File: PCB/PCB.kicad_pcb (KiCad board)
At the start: 4 copper layers, 54 x 29 mm, 80 parts, among them J1 USB_B_Micro, Q1 PJA3428, Q2 PJA3428, Q3 AO3401A, SW1 SW_Push, SW2 SW_Push, SW3 SW_Push, SW4 ON/OFF, U1 ESP32-PICO-MINI-02, U2 CP2102N-Axx-xQFN24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

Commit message: label btns and tps
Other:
- board text added: "BATT+"
- board text added: "BATT-"
- board text added: "CTS"
- board text added: "DTR"
- board text added: "GPIO0"
- board text added: "RESET"
- board text added: "RTS"
- board text added: "RX"
- board text added: "SCL"
- board text added: "SDA"
- board text added: "TX"
- board text added: "VIN"
- board text added: "~{INT}"
- board text added: "~{RESET}"

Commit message: silky touch ups
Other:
- board text added: "ECE477 Fall 2022 - Team 13 Brayden McNamara Ethan Crocker Kenzie Rappe Sean Boltjes"
- board text added: "Last Modified: 10/03/2022"
- board text added: "X"
- board text added: "Y"
- board text added: "Z"
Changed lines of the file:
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@@
   (gr_circle (center 225.725 102.425) (end 225.775 102.5) (layer "B.SilkS") (width 0.15) (fill none))
   (gr_circle (center 225.8 107.075) (end 225.9 107.1) (layer "B.SilkS") (width 0.15) (fill none))
+  (gr_line (start 240.853993 110.35) (end 240.403993 110) (layer "F.SilkS") (width 0.15))
+  (gr_line (start 238.603993 108.725) (end 238.803993 108.55) (layer "F.SilkS") (width 0.15))
+  (gr_circle (center 238.803993 110.35) (end 239.303993 111.5) (layer "F.SilkS") (width 0.15) (fill none))
+  (gr_line (start 238.803993 108.775) (end 238.803993 108.325) (layer "F.SilkS") (width 0.15))
+  (gr_line (start 240.603993 110.45) (end 240.453993 110.5) (layer "F.SilkS") (width 0.15))
+  (gr_line (start 240.403993 110.05) (end 240.403993 110) (layer "F.SilkS") (width 0.15))
+  (gr_line (start 240.453993 110.5) (end 240.628993 110.35) (layer "F.SilkS") (width 0.15))
   (gr_circle (center 235.025 107.85) (end 235.125 107.9) (layer "F.SilkS") (width 0.15) (fill none))
+  (gr_line (start 238.953993 108.725) (end 238.803993 108.55) (layer "F.SilkS") (width 0.15))
+  (gr_line (start 240.082986 110.35) (end 240.378993 110.35) (layer "F.SilkS") (width 0.15))
+  (gr_line (start 240.403993 110.35) (end 240.403993 110.7) (layer "F.SilkS") (width 0.15))
+  (gr_line (start 238.503993 108.775) (end 238.453993 108.775) (layer "F.SilkS") (width 0.15))
+  (gr_line (start 240.453993 110.15) (end 240.628993 110.35) (layer "F.SilkS") (width 0.15))
+  (gr_line (start 238.903993 108.575) (end 238.953993 108.725) (layer "F.SilkS") (width 0.15))
+  (gr_line (start 240.403993 110.35) (end 240.853993 110.35) (layer "F.SilkS") (width 0.15))
+  (gr_line (start 240.403993 110.7) (end 240.403993 110.05) (layer "F.SilkS") (width 0.15))
+  (gr_line (start 240.853993 110.35) (end 240.403993 110.7) (layer "F.SilkS") (width 0.15))
+  (gr_line (start 238.803993 108.325) (end 239.153993 108.775) (layer "F.SilkS") (width 0.15))
+  (gr_line (start 238.803993 108.775) (end 239.153993 108.775) (layer "F.SilkS") (width 0.15))
+  (gr_line (start 238.803993 109.096007) (end 238.803993 108.8) (layer "F.SilkS") (width 0.15))
+  (gr_line (start 238.803993 108.325) (end 238.453993 108.775) (layer "F.SilkS") (width 0.15))
+  (gr_line (start 239.153993 108.775) (end 238.503993 108.775) (layer "F.SilkS") (width 0.15))
   (gr_line (start 245.649999 119.199999) (end 245.65 92.16) (layer "Edge.Cuts") (width 0.2))
   (gr_arc (start 245.649999 119.199999) (mid 245.357106 119.907106) (end 244.649999 120.199999) (layer "Edge.Cuts") (width 0.2))
@@
   (gr_line (start 244.65 91.2) (end 192.65 91.2) (layer "Edge.Cuts") (width 0.2))
   (gr_line (start 191.65 92.2) (end 191.65 119.2) (layer "Edge.Cuts") (width 0.2))
+  (gr_text "ECE477 Fall 2022 - Team 13\nBrayden McNamara\nEthan Crocker\nKenzie Rappe\nSean Boltjes" (at 220.9 116.15) (layer "B.SilkS")
+    (effects (font (size 0.9 0.9) (thickness 0.2)) (justify left mirror))
+  )
   (gr_text "~{INT}" (at 205.2 117.55) (layer "B.SilkS")
     (effects (font (size 0.7 0.7) (thickness 0.15)))
@@
   (gr_text "CTS\n" (at 230.35 104.15) (layer "B.SilkS")
     (effects (font (size 0.7 0.7) (thickness 0.15)))
+  )
+  (gr_text "Last Modified: 10/03/2022" (at 230.1 119.05) (layer "B.SilkS")
+    (effects (font (size 0.8 0.8) (thickness 0.15)) (justify mirror))
   )
   (gr_text "SCL\n" (at 202.55 107) (layer "F.SilkS")
@@
     (effects (font (size 0.7 0.7) (thickness 0.15)))
   )
+  (gr_text "Z" (at 238.803993 110.4) (layer "F.SilkS")
+    (effects (font (size 1.5 1.5) (thickness 0.25)))
+  )
   (gr_text "TX\n" (at 233.9 112.55) (layer "F.SilkS")
     (effects (font (size 0.7 0.7) (thickness 0.15)))
@@
     (effects (font (size 0.7 0.7) (thickness 0.15)))
   )
+  (gr_text "Y\n" (at 238.803993 107.25) (layer "F.SilkS")
+    (effects (font (size 1.5 1.5) (thickness 0.25)))
+  )
+  (gr_text "X" (at 241.453993 110.4) (layer "F.SilkS")
+    (effects (font (size 1.5 1.5) (thickness 0.25)))
+  )
   (gr_text "GPIO0" (at 222.6 100.45) (layer "F.SilkS")

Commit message: buck-boost delete
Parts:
- added R9: 100k, Resistor_SMD:R_0603_1608Metric, F.Cu at (218.0, 94.0)
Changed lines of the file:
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@@
   (net 74 "unconnected-(U1-Pad19)")
   (net 75 "unconnected-(U1-Pad24)")
+  (net 76 "Net-(U4-Pad8)")
   (footprint "Button_Switch_THT:SW_Tactile_SPST_Angled_PTS645Vx58-2LFS" (layer "F.Cu")
     (at 242.59 117.42 180)
@@
       (offset (xyz 0 0 0))
       (scale (xyz 1 1 1))
+      (rotate (xyz 0 0 0))
+    )
+  )
+  (footprint "Resistor_SMD:R_0603_1608Metric" (layer "F.Cu")
+    (at 218 94)
+    (descr "Resistor SMD 0603 (1608 Metric), square (rectangular) end terminal, IPC_7351 nominal, (Body size source: IPC-SM-782 page 72, https://www.pcb-3d.com/wordpress/wp-content/uploads/ipc-sm-782a_amendment_1_and_2.pdf), generated with kicad-footprint-generator")
+    (tags "resistor")
+    (property "Sheetfile" "PCB.kicad_sch")
+    (property "Sheetname" "")
+    (attr smd)
+    (fp_text reference "R9" (at 0 -1.43) (layer "F.SilkS")
+      (effects (font (size 1 1) (thickness 0.15)))
+    )
+    (fp_text value "100k" (at 0 1.43) (layer "F.Fab")
+      (effects (font (size 1 1) (thickness 0.15)))
+    )
+    (fp_text user "${REFERENCE}" (at 0 0) (layer "F.Fab")
+      (effects (font (size 0.4 0.4) (thickness 0.06)))
+    )
+    (fp_line (start -0.237258 0.5225) (end 0.237258 0.5225) (layer "F.SilkS") (width 0.12))
+    (fp_line (start -0.237258 -0.5225) (end 0.237258 -0.5225) (layer "F.SilkS") (width 0.12))
+    (fp_line (start -1.48 0.73) (end -1.48 -0.73) (layer "F.CrtYd") (width 0.05))
+    (fp_line (start 1.48 0.73) (end -1.48 0.73) (layer "F.CrtYd") (width 0.05))
+    (fp_line (start 1.48 -0.73) (end 1.48 0.73) (layer "F.CrtYd") (width 0.05))
+    (fp_line (start -1.48 -0.73) (end 1.48 -0.73) (layer "F.CrtYd") (width 0.05))
+    (fp_line (start -0.8 0.4125) (end -0.8 -0.4125) (layer "F.Fab") (width 0.1))
+    (fp_line (start 0.8 0.4125) (end -0.8 0.4125) (layer "F.Fab") (width 0.1))
+    (fp_line (start -0.8 -0.4125) (end 0.8 -0.4125) (layer "F.Fab") (width 0.1))
+    (fp_line (start 0.8 -0.4125) (end 0.8 0.4125) (layer "F.Fab") (width 0.1))
+    (pad "1" smd roundrect (at -0.825 0) (size 0.8 0.95) (layers "F.Cu" "F.Paste" "F.Mask") (roundrect_rratio 0.25)
+      (net 76 "Net-(U4-Pad8)") (pintype "passive"))
+    (pad "2" smd roundrect (at 0.825 0) (size 0.8 0.95) (layers "F.Cu" "F.Paste" "F.Mask") (roundrect_rratio 0.25)
+      (net 26 "Vin") (pintype "passive"))
+    (model "${KICAD6_3DMODEL_DIR}/Resistor_SMD.3dshapes/R_0603_1608Metric.wrl"
+      (offset (xyz 0 0 0))
+      (scale (xyz 1 1 1))

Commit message: buck-boost pcb
buck-boost added to pcb
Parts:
- added C12: 47uF, Capacitor_SMD:C_0603_1608Metric, F.Cu at (199.0, 100.0)
- added C13: 100nF, Capacitor_SMD:C_0603_1608Metric, F.Cu at (200.0, 95.0)
- added C14: 10uF, Capacitor_SMD:C_0603_1608Metric, F.Cu at (200.0, 97.5)
- added C17: 47uF, Capacitor_SMD:C_0603_1608Metric, F.Cu at (204.0, 97.5)
- added R10: 100k, Resistor_SMD:R_0603_1608Metric, F.Cu at (208.0, 97.5)
- added R12: 34.8k, Resistor_SMD:R_0603_1608Metric, F.Cu at (195.0, 100.0)
- added R13: 309k, Resistor_SMD:R_0603_1608Metric, F.Cu at (203.0, 100.0)
- added R14: 100k, Resistor_SMD:R_0603_1608Metric, F.Cu at (208.0, 95.0)
- added R9: 100k, Resistor_SMD:R_0603_1608Metric, F.Cu at (204.0, 95.0)
- added U4: TPS63070RNMR, TPS63070RNMR:VREG_TPS63070RNMR, F.Cu at (195.7, 96.2)
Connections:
- C1 pad 2: GND -> Vin
- C10 pad 2: GND -> Vin
- C11 pad 2: GND -> Vin
- C15 pad 2: GND -> Vin
- C16 pad 2: GND -> Vin
- C18 pad 2: GND -> Vin
- C19 pad 2: GND -> Vin
- C2 pad 2: GND -> Vin
- C20 pad 2: GND -> Vin
- C21 pad 2: GND -> Vin
- C22 pad 1: GND -> Vin
- C23 pad 1: GND -> Vin
- C24 pad 1: GND -> Vin
- C25 pad 2: GND -> Vin
- C3 pad 2: GND -> Vin
- C4 pad 2: GND -> Vin
- C5 pad 2: GND -> Vin
- C6 pad 2: GND -> Vin
- C7 pad 1: GND -> Vin
- C8 pad 1: GND -> Vin
- C9 pad 2: GND -> Vin
- D1 pad 1: GND -> Vin
- D5 pad 1: GND -> Vin
- D6 pad 4: GND -> Vin
- J1 pad 5: GND -> Vin
- J1 pad 6: GND -> Vin
- Q3 pad 1: GND -> Vin
- R20 pad 1: GND -> Vin
- R27 pad 2: GND -> Vin
- R3 pad 1: GND -> Vin
- R6 pad 2: GND -> Vin
- SW1 pad 1: GND -> Vin
- SW2 pad 1: GND -> Vin
- SW3 pad 2: GND -> Vin
- TP9 pad 1: GND -> Vin
- U1 pad 1: GND -> Vin
- U1 pad 11: GND -> Vin
- U1 pad 14: GND -> Vin
- U1 pad 2: GND -> Vin
- U1 pad 36: GND -> Vin
- U1 pad 37: GND -> Vin
- U1 pad 38: GND -> Vin
- U1 pad 39: GND -> Vin
- U1 pad 40: GND -> Vin
- U1 pad 41: GND -> Vin
- U1 pad 42: GND -> Vin
- U1 pad 43: GND -> Vin
- U1 pad 44: GND -> Vin
- U1 pad 45: GND -> Vin
- U1 pad 46: GND -> Vin
- U1 pad 47: GND -> Vin
- U1 pad 48: GND -> Vin
- U1 pad 49: GND -> Vin
- U1 pad 50: GND -> Vin
- U1 pad 51: GND -> Vin
- U1 pad 52: GND -> Vin
- U1 pad 53: GND -> Vin
- U1 pad 54: GND -> Vin
- U1 pad 55: GND -> Vin
- U1 pad 56: GND -> Vin
- U1 pad 57: GND -> Vin
- U1 pad 58: GND -> Vin
- U1 pad 59: GND -> Vin
- U1 pad 60: GND -> Vin
- U1 pad 61: GND -> Vin
- U2 pad 2: GND -> Vin
- U2 pad 25: GND -> Vin
- U3 pad 1: GND -> Vin
- U3 pad 3: GND -> Vin
- U5 pad 10: GND -> Vin
- U5 pad 17: GND -> Vin
- U5 pad 2: GND -> Vin
- U5 pad 25: GND -> Vin
- U5 pad 5: GND -> Vin
- U5 pad 6: GND -> Vin
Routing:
- net Vin: track 9.02 -> 169.9 mm, vias 0 -> 23
- net GND: track 160.9 -> 0.00 mm, vias 23 -> 0
- added copper zone on In2.Cu, net Vin
- removed copper zone on In2.Cu, net GND

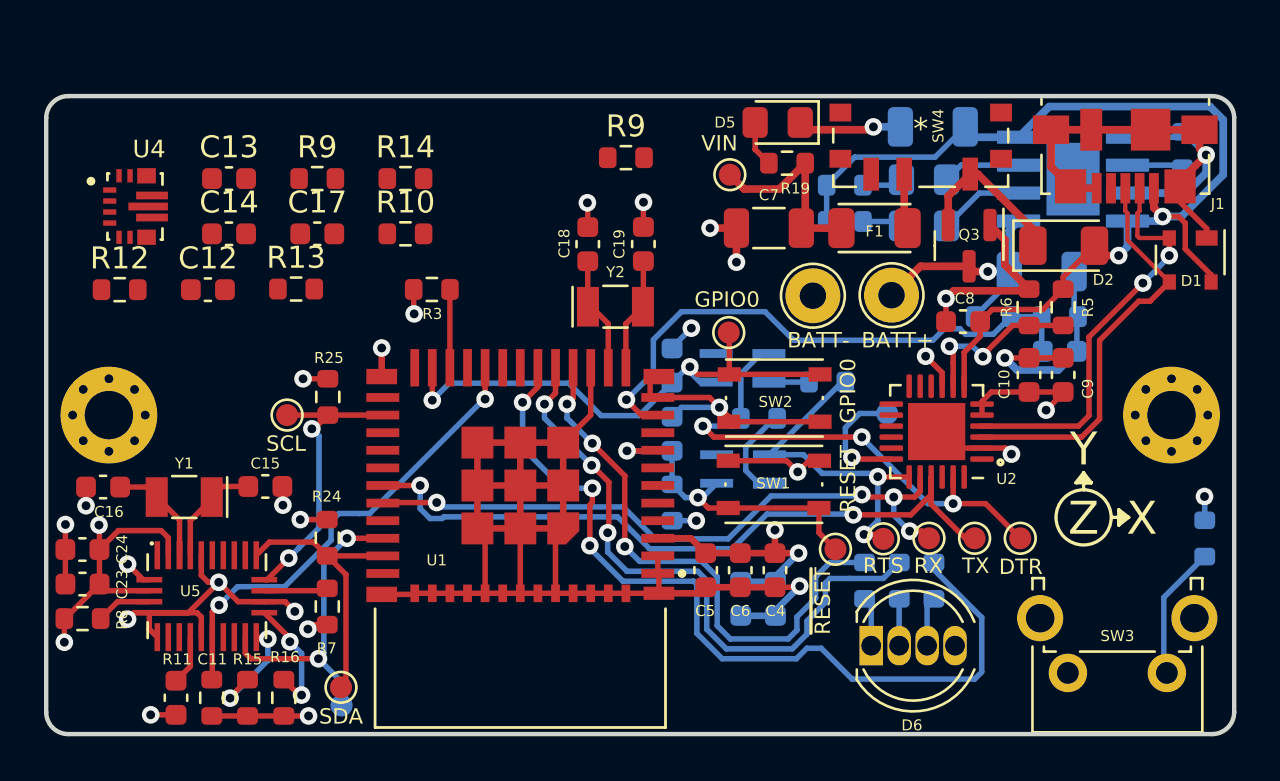
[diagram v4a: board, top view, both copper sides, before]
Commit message: updates based on in lab feedback and errors
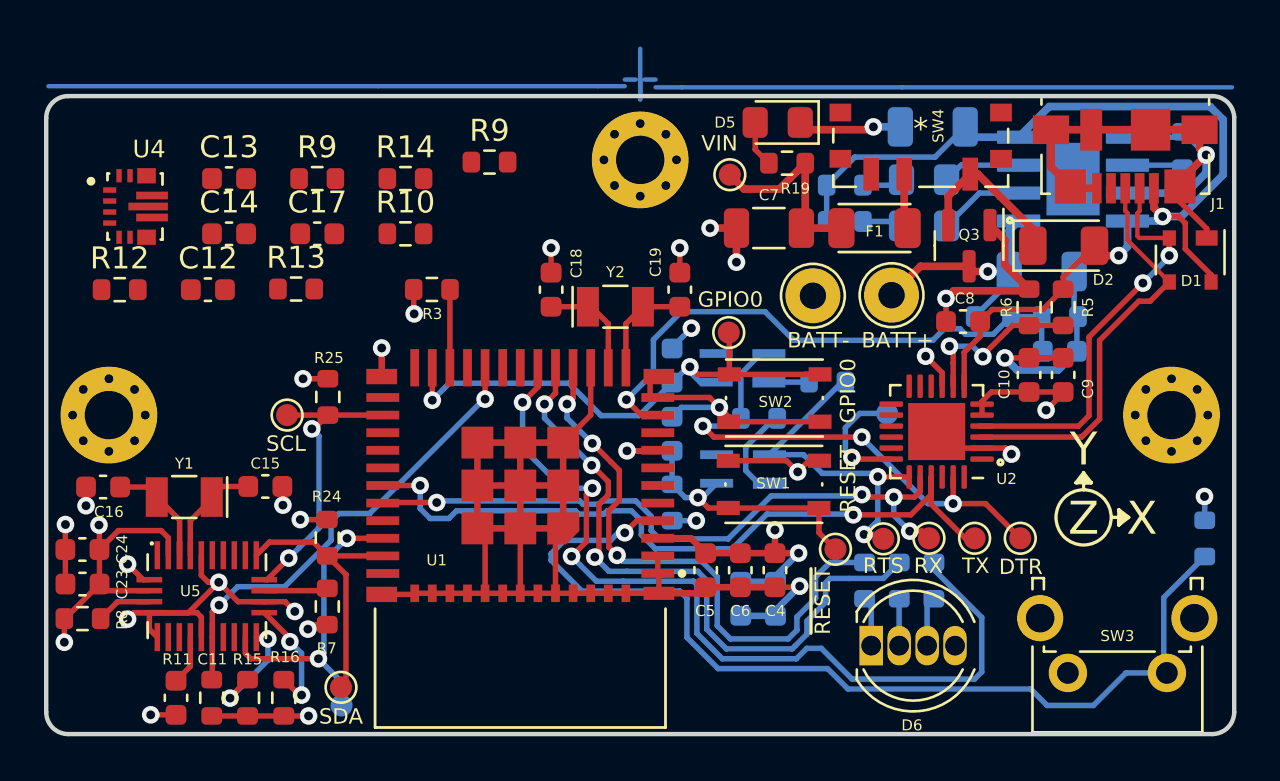
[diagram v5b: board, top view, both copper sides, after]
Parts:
- added H3: MountingHole, MountingHole:MountingHole_2.2mm_M2_Pad_Via, F.Cu at (218.7, 94.1)
- moved R9 6.20 mm to (211.8, 94.2)
- moved C18 2.66 mm to (214.6, 100.0)
- moved C19 2.65 mm to (220.4, 100.0)
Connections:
- C1 pad 2: Vin -> GND
- C10 pad 2: Vin -> GND
- C11 pad 2: Vin -> GND
- C12 pad 1: Vin -> GND
- C12 pad 2: Vin -> GND
- C13 pad 2: Vin -> GND
- C14 pad 2: Vin -> GND
- C15 pad 2: Vin -> GND
- C16 pad 2: Vin -> GND
- C17 pad 2: Vin -> GND
- C18 pad 2: Vin -> GND
- C19 pad 2: Vin -> GND
- C2 pad 2: Vin -> GND
- C20 pad 2: Vin -> GND
- C21 pad 2: Vin -> GND
- C22 pad 1: Vin -> GND
- C23 pad 1: Vin -> GND
- C24 pad 1: Vin -> GND
- C25 pad 2: Vin -> GND
- C3 pad 2: Vin -> GND
- C4 pad 2: Vin -> GND
- C5 pad 2: Vin -> GND
- C6 pad 2: Vin -> GND
- C7 pad 1: Vin -> GND
- C8 pad 1: Vin -> GND
- C9 pad 2: Vin -> GND
- D1 pad 1: Vin -> GND
- D5 pad 1: Vin -> GND
- D6 pad 4: Vin -> GND
- J1 pad 5: Vin -> GND
- J1 pad 6: Vin -> GND
- Q3 pad 1: Vin -> GND
- R10 pad 1: Vin -> GND
- R12 pad 1: Vin -> GND
- R20 pad 1: Vin -> GND
- R27 pad 2: Vin -> GND
- R3 pad 1: Vin -> GND
- R6 pad 2: Vin -> GND
- R9 pad 2: Vin -> GND
- SW1 pad 1: Vin -> GND
- SW2 pad 1: Vin -> GND
- SW3 pad 2: Vin -> GND
- TP9 pad 1: Vin -> GND
- U1 pad 1: Vin -> GND
- U1 pad 11: Vin -> GND
- U1 pad 14: Vin -> GND
- U1 pad 2: Vin -> GND
- U1 pad 36: Vin -> GND
- U1 pad 37: Vin -> GND
- U1 pad 38: Vin -> GND
- U1 pad 39: Vin -> GND
- U1 pad 4: unconnected-(U1-Pad4) -> SESSION_BUTTON
- U1 pad 40: Vin -> GND
- U1 pad 41: Vin -> GND
- U1 pad 42: Vin -> GND
- U1 pad 43: Vin -> GND
- U1 pad 44: Vin -> GND
- U1 pad 45: Vin -> GND
- U1 pad 46: Vin -> GND
- U1 pad 47: Vin -> GND
- U1 pad 48: Vin -> GND
- U1 pad 49: Vin -> GND
- U1 pad 50: Vin -> GND
- U1 pad 51: Vin -> GND
- U1 pad 52: Vin -> GND
- U1 pad 53: Vin -> GND
- U1 pad 54: Vin -> GND
- U1 pad 55: Vin -> GND
- U1 pad 56: Vin -> GND
- U1 pad 57: Vin -> GND
- U1 pad 58: Vin -> GND
- U1 pad 59: Vin -> GND
- U1 pad 60: Vin -> GND
- U1 pad 61: Vin -> GND
- U2 pad 2: Vin -> GND
- U2 pad 25: Vin -> GND
- U3 pad 1: Vin -> GND
- U3 pad 3: Vin -> GND
- U4 pad 1: Vin -> GND
- U4 pad 10: Vin -> GND
- U4 pad 12_13: Vin -> GND
- U4 pad 15: Vin -> GND
- U4 pad 4: Vin -> GND
- U4 pad 6: Vin -> GND
- U5 pad 10: Vin -> GND
- U5 pad 17: Vin -> GND
- U5 pad 2: Vin -> GND
- U5 pad 25: Vin -> GND
- U5 pad 5: Vin -> GND
- U5 pad 6: Vin -> GND
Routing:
- net GND: track 0.00 -> 160.9 mm, vias 0 -> 23
- net Vin: track 169.9 -> 9.02 mm, vias 23 -> 0
- net SESSION_BUTTON: track 6.12 -> 44.3 mm, vias 0 -> 1
- net RGB_BLUE: track 38.6 -> 40.0 mm
- net RGB_GREEN: track 28.7 -> 29.6 mm
- net PROG_RX: track 29.3 -> 30.1 mm
- net RGB_RED: track 25.6 -> 26.5 mm
- net PROG_TX: track 32.1 -> 32.9 mm
- added copper zone on In2.Cu, net GND
- removed copper zone on In2.Cu, net Vin
